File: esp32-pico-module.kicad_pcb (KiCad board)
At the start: 2 copper layers, 20.6 x 15.6 mm, 11 parts, among them J1 Conn_01x08_Male, J2 Conn_01x08_Male, U1 ESP32_PICO_V3, U2 Trace

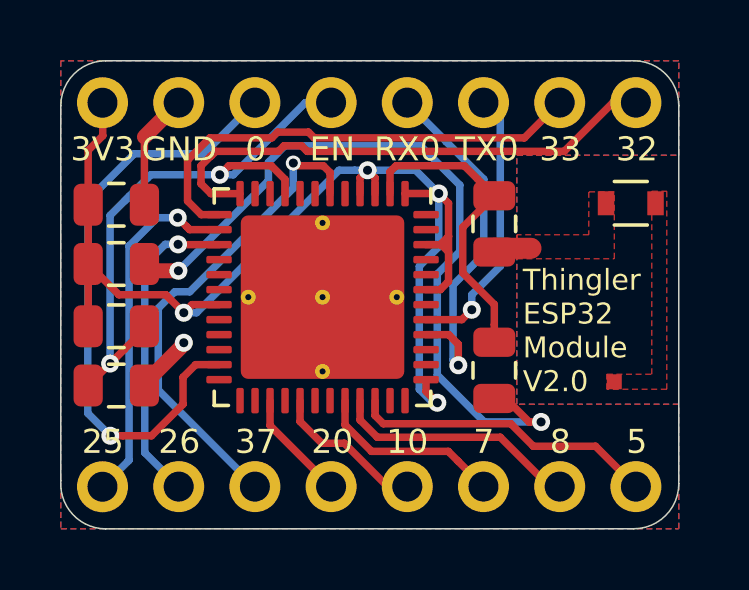
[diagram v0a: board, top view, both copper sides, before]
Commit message: Removed extra impedance components for the antenna
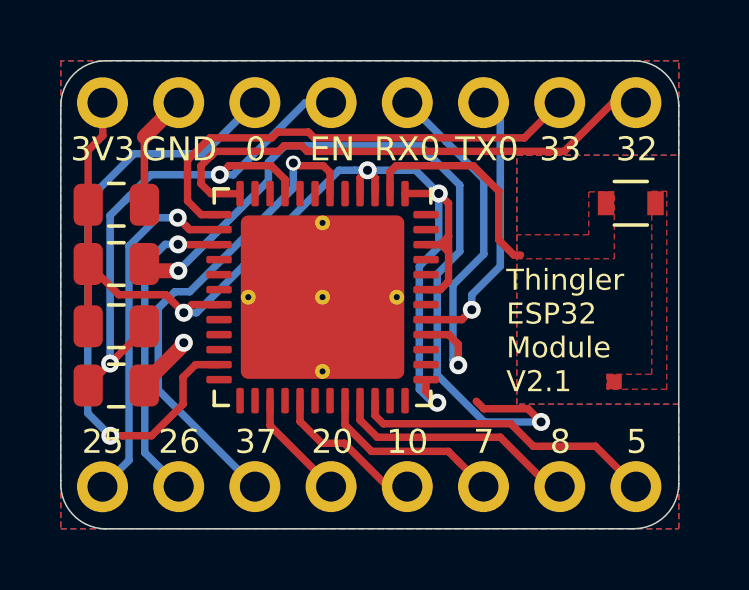
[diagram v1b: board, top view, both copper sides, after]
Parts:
- removed C3: 8.2p, Capacitor_SMD:C_0805_2012Metric
- removed L1: 1.5n, Inductor_SMD:L_0805_2012Metric
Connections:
- U1 pad 2: Net-(C3-Pad1) -> Net-(AE1-Pad1)
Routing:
- net Net-(C3-Pad1): track 10.5 -> 0.00 mm
- net Net-(AE1-Pad1): track 1.23 -> 7.35 mm
- net Earth: track 31.7 -> 32.3 mm
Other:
- board text added: "Thingler ESP32 Module V2.1"
- board text removed: "Thingler ESP32 Module V2.0"
